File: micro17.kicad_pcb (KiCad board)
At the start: 4 copper layers, 20 x 30 mm, 92 parts, among them J1 Conn_01x05, J2 AXK640347YG, J4 USB_B_Micro, U1 STM32G473CCUx, U2 XC6220B331MR, U3 CPC1117N, U4 MCP6002, U5 MCP4451-503-ST, U6 MCP6002, U7 MCP6002, Y1 8 MHz

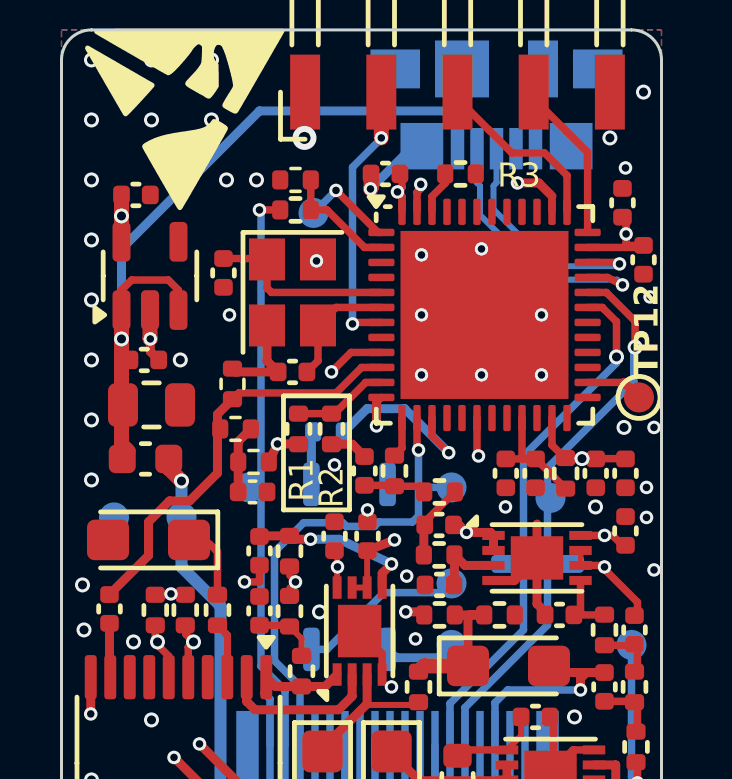
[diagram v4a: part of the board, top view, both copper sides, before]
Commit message: Changed PA2 bias circuit
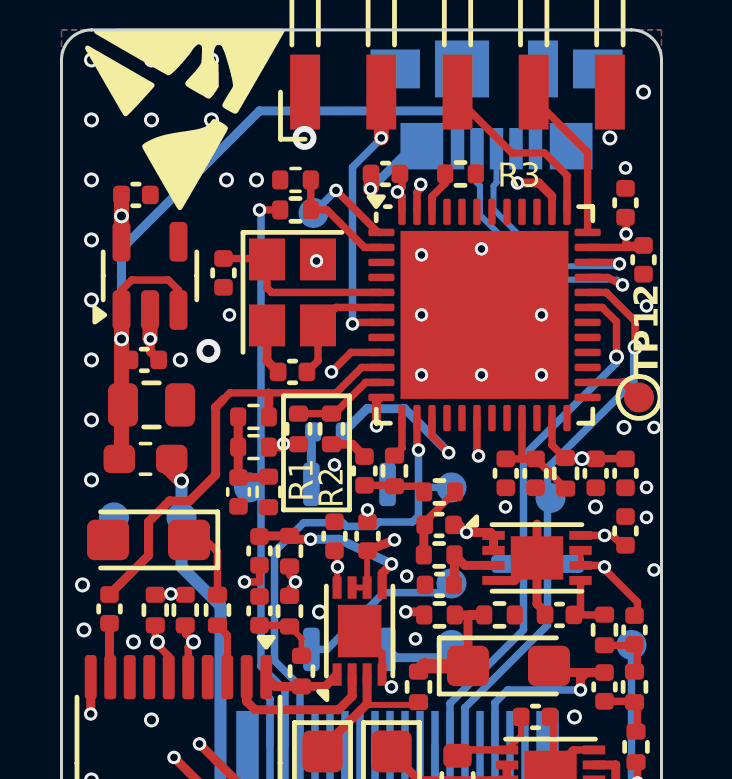
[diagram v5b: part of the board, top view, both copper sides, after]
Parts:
- FB1: footprint Capacitor_SMD:C_0603_1608Metric -> Inductor_SMD:L_0603_1608Metric_Pad1.05x0.95mm_HandSolder
- R26: value 10k -> 22k
- R28: value 12k -> 22k
- moved R27 3.79 mm to (186.9, 65.4), turned to -90 degrees
- moved R28 1.50 mm to (186.4, 62.9), turned to 180 degrees
- moved R26 0.85 mm to (186.4, 63.9)
- moved C12 0.47 mm to (185.9, 65.4), turned to -90 degrees
- moved C3 0.10 mm to (198.8, 55.8)
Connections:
- R26 pad 1: Net-(C12-Pad1) -> +3V3
- R26 pad 2: AUDIO_IN_FILT -> Net-(C12-Pad1)
- R27 pad 1: AUDIO_IN_FILT -> Net-(C12-Pad1)
- R28 pad 1: Net-(C12-Pad1) -> AUDIO_IN_FILT
- R28 pad 2: +3V3 -> Net-(C12-Pad1)
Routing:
- net GND: track 37.2 -> 35.6 mm, vias 60 -> 61
- net AUDIO_IN_FILT: track 14.0 -> 15.0 mm
- net Net-(C12-Pad1): track 2.27 -> 3.00 mm

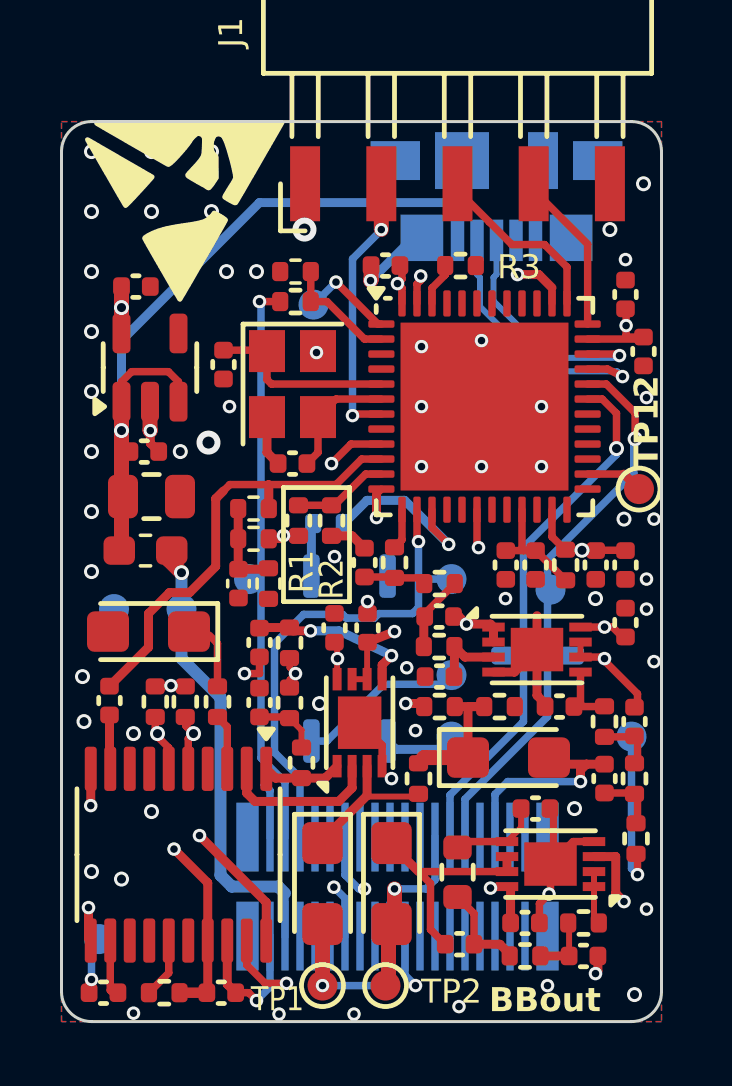
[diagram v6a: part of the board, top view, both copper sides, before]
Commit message: Bias voltage changed, usart rx tp add
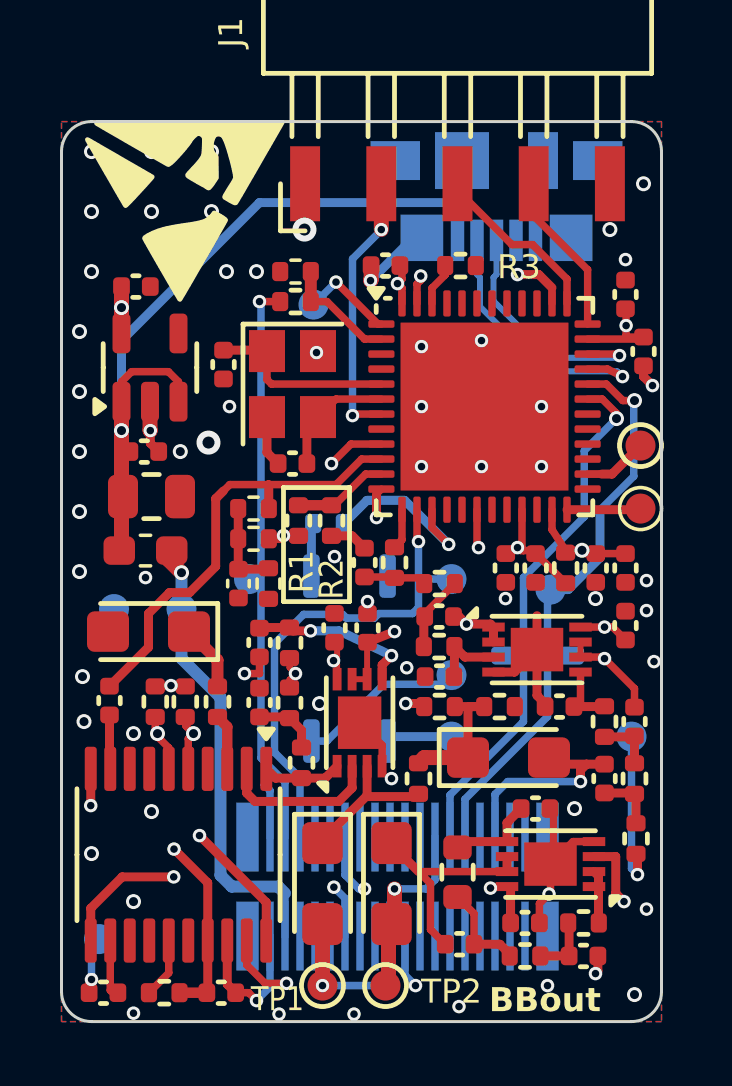
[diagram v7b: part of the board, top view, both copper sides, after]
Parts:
- added TP14: GP, TestPoint:TestPoint_Pad_D1.0mm, F.Cu at (199.3, 62.9)
- moved TP12 1.45 mm to (199.3, 60.8)
- moved C30 0.10 mm to (198.8, 66.8)
- moved C5 0.10 mm to (198.8, 64.9)
- moved C7 0.10 mm to (197.8, 64.9)
- moved C8 0.10 mm to (194.8, 64.9)
- moved C9 0.10 mm to (195.8, 64.9)
- moved R5 0.10 mm to (196.8, 64.9)
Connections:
- C8 pad 1: /MCU/VDDA -> VDDA
- C9 pad 2: /MCU/VDDA -> VDDA
- R1 pad 2: +3V3 -> VDDA
- R20 pad 1: +5V -> VDDA
- R26 pad 1: +3V3 -> VDDA
- R5 pad 1: /MCU/VDDA -> VDDA
- U1 pad 21: /MCU/VDDA -> VDDA
- U1 pad 22: unconnected-(U1-PB10-Pad22) -> USART3_TX
- U1 pad 24: unconnected-(U1-PB11-Pad24) -> USART3_RX
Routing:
- net VDDA: track 0.00 -> 19.7 mm, vias 0 -> 3
- net /MCU/VDDA: track 3.80 -> 0.00 mm
- net USART3_RX: track 0.00 -> 2.47 mm
- net +3V3: track 69.1 -> 68.3 mm, vias 8 -> 7
- net GND: track 35.6 -> 36.4 mm, vias 61 -> 60
- net MCU_RX: track 19.2 -> 19.7 mm
- net +5V: track 58.8 -> 59.0 mm, vias 5 -> 4
- net Net-(U5A-P0A): track 20.4 -> 20.5 mm, vias 3 -> 2

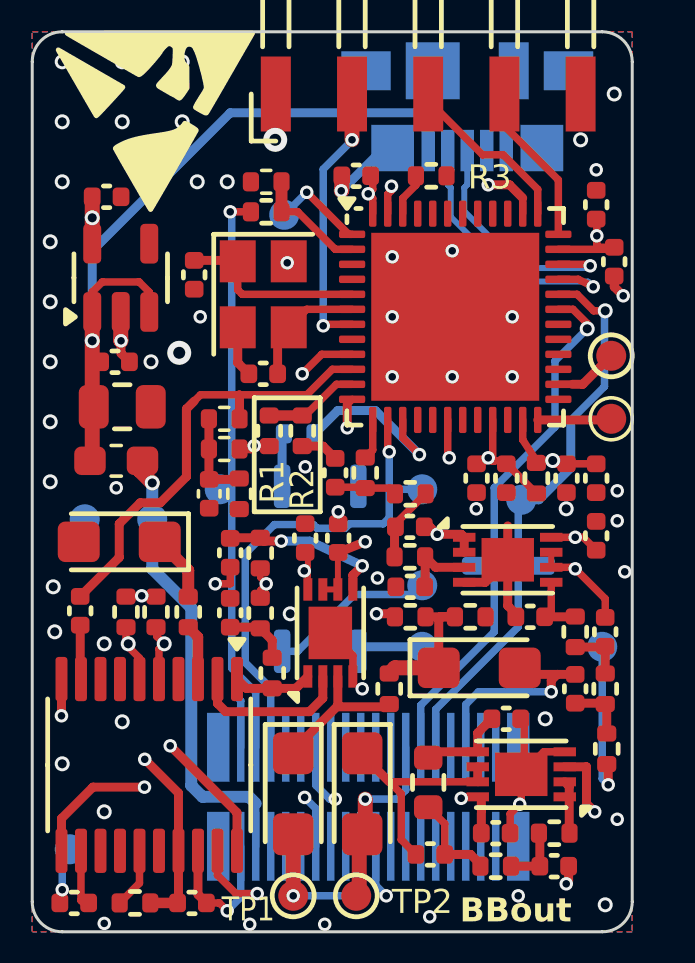
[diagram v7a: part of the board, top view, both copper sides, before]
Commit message: R30 Added
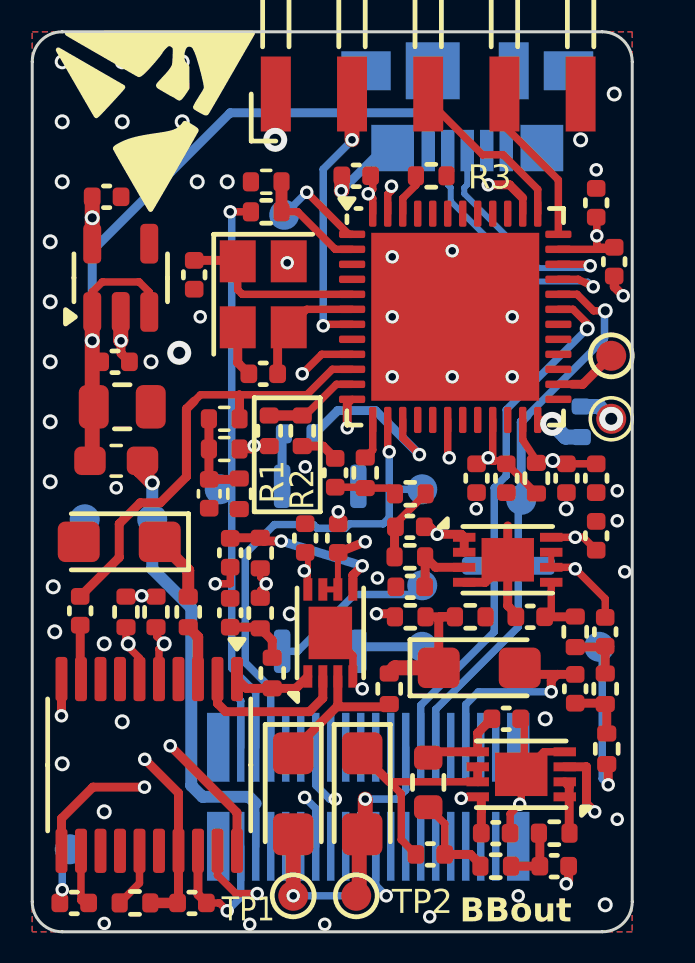
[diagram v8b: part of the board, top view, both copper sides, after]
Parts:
- added R30: 10k, Resistor_SMD:R_0402_1005Metric, B.Cu at (198.3, 63.0)
- moved TP8 0.10 mm to (198.9, 70.5)
- moved C3 0.06 mm to (198.8, 55.7)
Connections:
- TP14 pad 1: USART3_RX -> Net-(R30-Pad2)
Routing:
- net +3V3: track 68.3 -> 67.0 mm
- net Net-(R30-Pad2): track 0.00 -> 1.22 mm, vias 0 -> 1
- net USART3_RX: track 2.47 -> 1.69 mm, vias 0 -> 1
